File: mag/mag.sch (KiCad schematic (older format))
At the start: 17 parts

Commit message: есть схема макета, начал распологать элементы
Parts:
- removed VD? (x2): S13_SOD-123, N_VD_HL:Диод_S13_SOD-123, symbol elements:Диод_шоттки
- added C5: 10мкФ_0603, N_RLC:Конденсатор_SMD_0603, symbol elements:Конденсатор_керамический
- added K1, K2: кнопка_FSMSM, N_X:Кнопка_FSMSM, symbol elements:кнопка
- added R3, R4, R5: 20k_0603, N_RLC:Конденсатор_SMD_0603, symbol elements:Резистор_0,065Вт
- added VD1: display_EDS803_EDS805, N_VD_HL:display_EDS803_805, symbol elements:display_EDS803_EDS805
- added XP1: Вилка_PLS3, N_X:Розетка_PBS3_вертикальная, symbol elements:Вилка_PLS3
- added XP2: Вилка_PLS6, N_X:Вилка_PLS6_вертикальная, symbol elements:Вилка_PLS6
- DD2, DD3, DD4, DD5: renamed from DD?; value D-triger_8bit -> D-triger_74VHC573MTC
- XS1: renamed from XS?; value Розетка_PBS4 -> oled_0.91_128x32; footprint (none) -> N_VD_HL:oled_0.91_128x32
- XS2: renamed from XS?; footprint (none) -> N_X:Вилка_PLS4_вертикальная
- XТ1: renamed from XТ?; footprint N_X:Клеммник_х2_шаг2.54 -> N_X:батарейный_отсек_CR2032
- gave numbers to parts that had none: 8
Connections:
- net labels added: ADC6, AREF, MC_RX, MC_TX, Out11, Out12, Out13, Out14, Out15, Out16, Out17, Out18, Out21, Out22, Out23, Out24, Out25, Out26, Out27, Out28, Out31, Out32, Out33, Out34, Out35, Out36, Out37, Out38, Out41, Out42, Out43, Out44, Out45, Out46, Out47, Out48, PC0, PC1, PC2, PC3, PD2, PD3, PD4, VCC_bat, VCC_prog
- wire segments 101 -> 207
- no-connect marks 0 -> 5
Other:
- note added: "Информация"
- note added: "Режим/Работа"
- moved on the sheet: C1, C2, C3, C4, DD1, R1, R2, XP3, XТ1

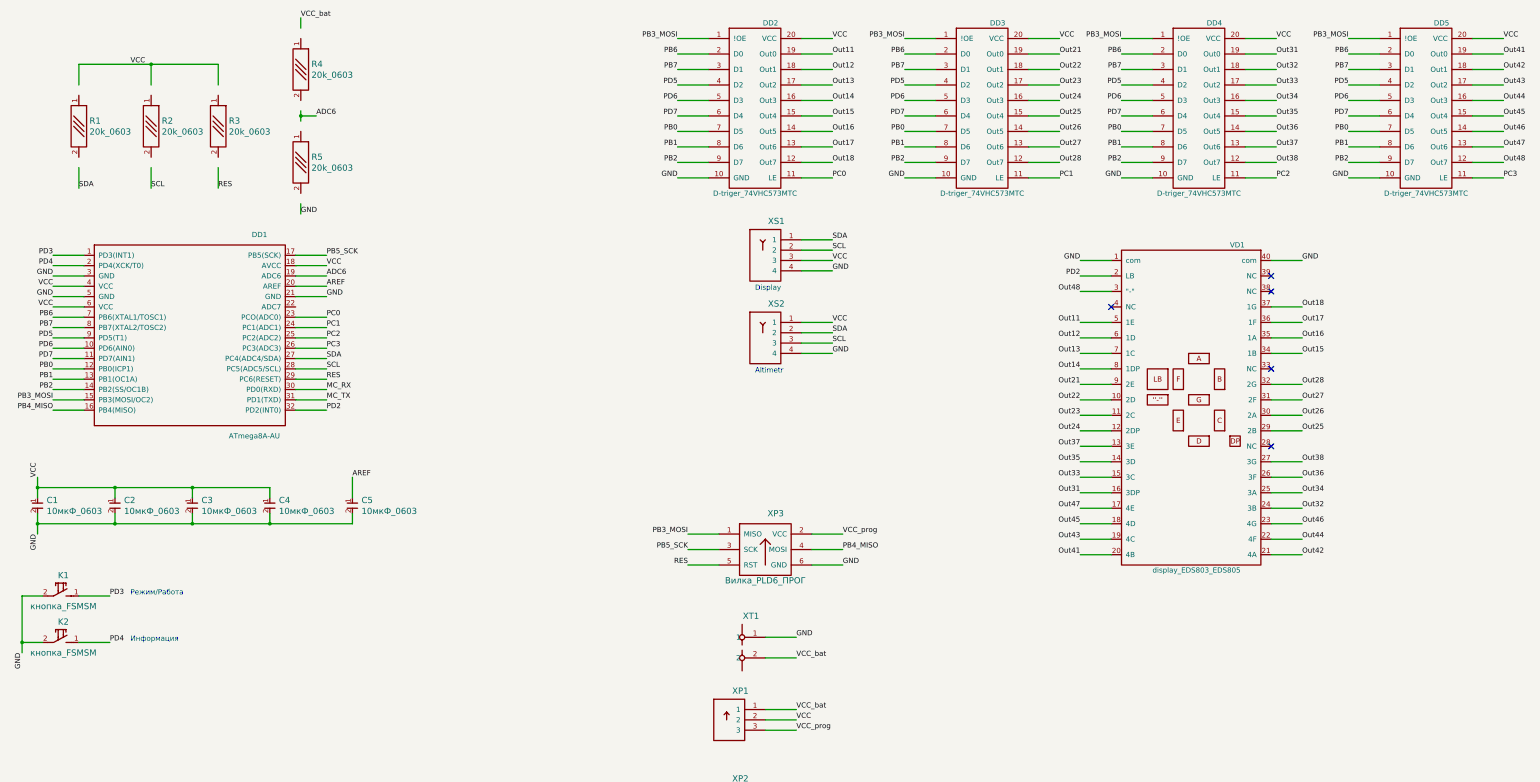
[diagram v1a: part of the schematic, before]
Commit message: есть топология и габарит, не расставлен обвес
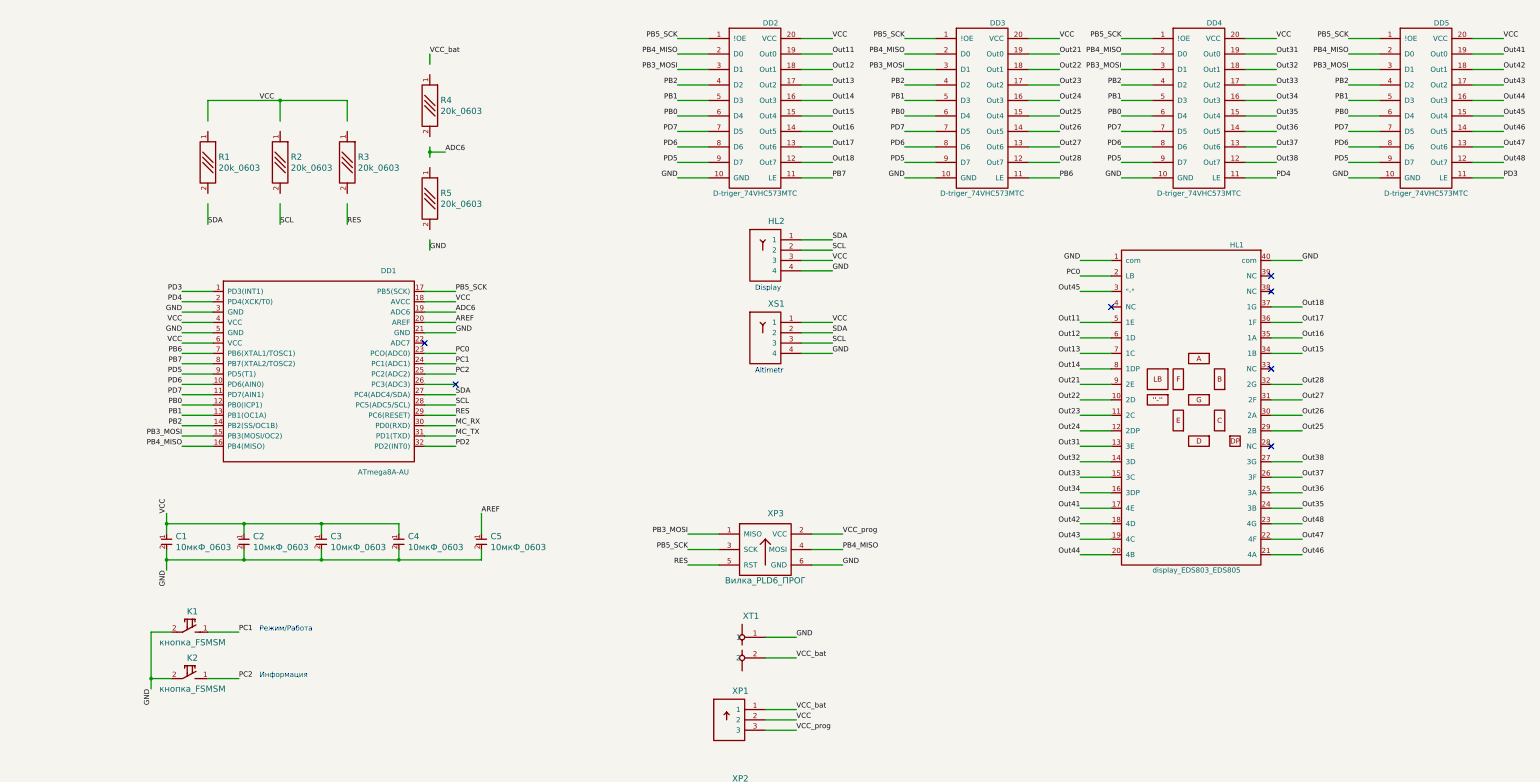
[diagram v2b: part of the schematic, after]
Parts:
- renumbered VD1 to HL1, XS1 to HL2, XS2 to XS1
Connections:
- net labels removed: PC3
- no-connect marks 5 -> 7
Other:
- moved on the sheet: C1, C2, C3, C4, C5, DD1, K1, K2, R1, R2, R3, R4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

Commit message: закончена трассировка и маркировка
не подготавливались файлы производства
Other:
- moved on the sheet: DD2, DD3
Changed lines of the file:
@@
 L elements:D-triger_8bit DD2
 U 1 1 5CE49B21
-P 8200 950
-F 0 "DD2" H 8600 1100 50  0000 C CNN
-F 1 "D-triger_74VHC573MTC" H 8450 -550 50  0000 C CNN
-F 2 "N_DD:SSOP-20" H 8200 950 50  0001 C CNN
-F 3 "" H 8200 950 50  0001 C CNN
-	1    8200 950
+P 8100 950
+F 0 "DD2" H 8500 1100 50  0000 C CNN
+F 1 "D-triger_74VHC573MTC" H 8350 -550 50  0000 C CNN
+F 2 "N_DD:SSOP-20" H 8100 950 50  0001 C CNN
+F 3 "" H 8100 950 50  0001 C CNN
+	1    8100 950
 	1    0    0    -1
 $EndComp
@@
 PB2
 Wire Wire Line
-	8000 1100 7700 1100
-Wire Wire Line
-	8000 1250 7700 1250
-Wire Wire Line
-	8000 1400 7700 1400
-Wire Wire Line
-	8000 1550 7700 1550
-Wire Wire Line
-	8000 1700 7700 1700
-Wire Wire Line
-	8000 1850 7700 1850
-Wire Wire Line
-	8000 2000 7700 2000
-Wire Wire Line
-	8000 2150 7700 2150
+	7900 1100 7600 1100
+Wire Wire Line
+	7900 1250 7600 1250
+Wire Wire Line
+	7900 1400 7600 1400
+Wire Wire Line
+	7900 1550 7600 1550
+Wire Wire Line
+	7900 1700 7600 1700
+Wire Wire Line
+	7900 1850 7600 1850
+Wire Wire Line
+	7900 2000 7600 2000
+Wire Wire Line
+	7900 2150 7600 2150
 Wire Wire Line
 	3200 3600 2900 3600
@@
 VCC
 Wire Wire Line
-	8000 2300 7700 2300
-Text Label 7700 2300 2    50   ~ 0
-GND
-Wire Wire Line
-	9200 950  8900 950
-Text Label 9200 950  0    50   ~ 0
-VCC
-Wire Wire Line
-	8000 950  7700 950
+	7900 2300 7600 2300
+Text Label 7600 2300 2    50   ~ 0
+GND
+Wire Wire Line
+	9100 950  8800 950
+Text Label 9100 950  0    50   ~ 0
+VCC
+Wire Wire Line
+	7900 950  7600 950
 Wire Wire Line
 	8900 2900 9200 2900
@@
 L elements:D-triger_8bit DD3
 U 1 1 5CE59956
-P 10400 950
-F 0 "DD3" H 10800 1100 50  0000 C CNN
-F 1 "D-triger_74VHC573MTC" H 10650 -550 50  0000 C CNN
-F 2 "N_DD:SSOP-20" H 10400 950 50  0001 C CNN
-F 3 "" H 10400 950 50  0001 C CNN
-	1    10400 950
-	1    0    0    -1
-$EndComp
-Wire Wire Line
-	10200 1100 9900 1100
-Wire Wire Line
-	10200 1250 9900 1250
-Wire Wire Line
-	10200 1400 9900 1400
-Wire Wire Line
-	10200 1550 9900 1550
-Wire Wire Line
-	10200 1700 9900 1700
-Wire Wire Line
-	10200 1850 9900 1850
-Wire Wire Line
-	10200 2000 9900 2000
-Wire Wire Line
-	10200 2150 9900 2150
-Wire Wire Line
-	10200 2300 9900 2300
-Wire Wire Line
-	11400 950  11100 950
-Text Label 11400 950  0    50   ~ 0
-VCC
-Wire Wire Line
-	10200 950  9900 950
+P 10300 950
+F 0 "DD3" H 10700 1100 50  0000 C CNN
+F 1 "D-triger_74VHC573MTC" H 10550 -550 50  0000 C CNN
+F 2 "N_DD:SSOP-20" H 10300 950 50  0001 C CNN
+F 3 "" H 10300 950 50  0001 C CNN
+	1    10300 950
+	1    0    0    -1
+$EndComp
+Wire Wire Line
+	10100 1100 9800 1100
+Wire Wire Line
+	10100 1250 9800 1250
+Wire Wire Line
+	10100 1400 9800 1400
+Wire Wire Line
+	10100 1550 9800 1550
+Wire Wire Line
+	10100 1700 9800 1700
+Wire Wire Line
+	10100 1850 9800 1850
+Wire Wire Line
+	10100 2000 9800 2000
+Wire Wire Line
+	10100 2150 9800 2150
+Wire Wire Line
+	10100 2300 9800 2300
+Wire Wire Line
+	11300 950  11000 950
+Text Label 11300 950  0    50   ~ 0
+VCC
+Wire Wire Line
+	10100 950  9800 950
 $Comp
 L elements:D-triger_8bit DD4
@@
 NoConn ~ 13450 4900
 Wire Wire Line
-	9200 1100 8900 1100
-Text Label 9200 1100 0    50   ~ 0
+	9100 1100 8800 1100
+Text Label 9100 1100 0    50   ~ 0
 Out11
 Wire Wire Line
-	9200 1250 8900 1250
-Text Label 9200 1250 0    50   ~ 0
+	9100 1250 8800 1250
+Text Label 9100 1250 0    50   ~ 0
 Out12
 Wire Wire Line
-	9200 1400 8900 1400
-Text Label 9200 1400 0    50   ~ 0
+	9100 1400 8800 1400
+Text Label 9100 1400 0    50   ~ 0
 Out13
 Wire Wire Line
-	9200 1550 8900 1550
-Text Label 9200 1550 0    50   ~ 0
+	9100 1550 8800 1550
+Text Label 9100 1550 0    50   ~ 0
 Out14
 Wire Wire Line
-	9200 1700 8900 1700
-Text Label 9200 1700 0    50   ~ 0
+	9100 1700 8800 1700
+Text Label 9100 1700 0    50   ~ 0
 Out15
 Wire Wire Line
-	9200 1850 8900 1850
-Text Label 9200 1850 0    50   ~ 0
+	9100 1850 8800 1850
+Text Label 9100 1850 0    50   ~ 0
 Out16
 Wire Wire Line
-	9200 2000 8900 2000
-Text Label 9200 2000 0    50   ~ 0
+	9100 2000 8800 2000
+Text Label 9100 2000 0    50   ~ 0
 Out17
 Wire Wire Line
-	9200 2150 8900 2150
-Text Label 9200 2150 0    50   ~ 0
+	9100 2150 8800 2150
+Text Label 9100 2150 0    50   ~ 0
 Out18
 Wire Wire Line
-	11400 1100 11100 1100
-Text Label 11400 1100 0    50   ~ 0
+	11300 1100 11000 1100
+Text Label 11300 1100 0    50   ~ 0
 Out21
 Wire Wire Line
-	11400 1250 11100 1250
-Text Label 11400 1250 0    50   ~ 0
+	11300 1250 11000 1250
+Text Label 11300 1250 0    50   ~ 0
 Out22
 Wire Wire Line
-	11400 1400 11100 1400
-Text Label 11400 1400 0    50   ~ 0
+	11300 1400 11000 1400
+Text Label 11300 1400 0    50   ~ 0
 Out23
 Wire Wire Line
-	11400 1550 11100 1550
-Text Label 11400 1550 0    50   ~ 0
+	11300 1550 11000 1550
+Text Label 11300 1550 0    50   ~ 0
 Out24
 Wire Wire Line
-	11400 1700 11100 1700
-Text Label 11400 1700 0    50   ~ 0
+	11300 1700 11000 1700
+Text Label 11300 1700 0    50   ~ 0
 Out25
 Wire Wire Line
-	11400 1850 11100 1850
-Text Label 11400 1850 0    50   ~ 0
+	11300 1850 11000 1850
+Text Label 11300 1850 0    50   ~ 0
 Out26
 Wire Wire Line
-	11400 2000 11100 2000
-Text Label 11400 2000 0    50   ~ 0
+	11300 2000 11000 2000
+Text Label 11300 2000 0    50   ~ 0
 Out27
 Wire Wire Line
-	11400 2150 11100 2150
-Text Label 11400 2150 0    50   ~ 0
+	11300 2150 11000 2150
+Text Label 11300 2150 0    50   ~ 0
 Out28
 Wire Wire Line
@@
 	13500 2300 13200 2300
 Wire Wire Line
-	11400 2300 11100 2300
-Wire Wire Line
-	9200 2300 8900 2300
+	11300 2300 11000 2300
+Wire Wire Line
+	9100 2300 8800 2300
 $Comp
 L elements:кнопка K1
@@
 Text Label 13750 4450 0    50   ~ 0
 Out27
-Text Label 7700 1250 2    50   ~ 0
+Text Label 7600 1250 2    50   ~ 0
 PB3_MOSI
-Text Label 7700 2150 2    50   ~ 0
+Text Label 7600 2150 2    50   ~ 0
 PD5
-Text Label 7700 2000 2    50   ~ 0
+Text Label 7600 2000 2    50   ~ 0
 PD6
-Text Label 7700 1850 2    50   ~ 0
+Text Label 7600 1850 2    50   ~ 0
 PD7
-Text Label 7700 1700 2    50   ~ 0
+Text Label 7600 1700 2    50   ~ 0
 PB0
-Text Label 7700 1550 2    50   ~ 0
+Text Label 7600 1550 2    50   ~ 0
 PB1
-Text Label 7700 1400 2    50   ~ 0
+Text Label 7600 1400 2    50   ~ 0
 PB2
-Text Label 7700 1100 2    50   ~ 0
+Text Label 7600 1100 2    50   ~ 0
 PB4_MISO
-Text Label 7700 950  2    50   ~ 0
+Text Label 7600 950  2    50   ~ 0
 PB5_SCK
-Text Label 9900 2300 2    50   ~ 0
-GND
-Text Label 9900 1250 2    50   ~ 0
+Text Label 9800 2300 2    50   ~ 0
+GND
+Text Label 9800 1250 2    50   ~ 0
 PB3_MOSI
-Text Label 9900 2150 2    50   ~ 0
+Text Label 9800 2150 2    50   ~ 0
 PD5
-Text Label 9900 2000 2    50   ~ 0
+Text Label 9800 2000 2    50   ~ 0
 PD6
-Text Label 9900 1850 2    50   ~ 0
+Text Label 9800 1850 2    50   ~ 0
 PD7
-Text Label 9900 1700 2    50   ~ 0
+Text Label 9800 1700 2    50   ~ 0
 PB0
-Text Label 9900 1550 2    50   ~ 0
+Text Label 9800 1550 2    50   ~ 0
 PB1
-Text Label 9900 1400 2    50   ~ 0
+Text Label 9800 1400 2    50   ~ 0
 PB2
-Text Label 9900 1100 2    50   ~ 0
+Text Label 9800 1100 2    50   ~ 0
 PB4_MISO
-Text Label 9900 950  2    50   ~ 0
+Text Label 9800 950  2    50   ~ 0
 PB5_SCK
 Text Label 12000 2300 2    50   ~ 0
@@
 Text Label 2900 4000 2    50   ~ 0
 PB6
-Text Label 11400 2300 0    50   ~ 0
+Text Label 11300 2300 0    50   ~ 0
 PB6
-Text Label 9200 2300 0    50   ~ 0
+Text Label 9100 2300 0    50   ~ 0
 PB7
 Text Label 2900 4100 2    50   ~ 0

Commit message: готово отображение на lcd
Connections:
- no-connect marks 7 -> 8
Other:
- note added: "поменять out44 и out45"
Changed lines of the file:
@@
 PC2
 NoConn ~ 5550 4300
+NoConn ~ 5850 4900
+Text Notes 14650 5900 0    50   ~ 0
+поменять out44 и out45
 $EndSCHEMATC

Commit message: подготавливается переделка под стационарные датчики
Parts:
- removed XТ1: Клеммник_х2, N_X:батарейный_отсек_CR2032, symbol elements:Клеммник_х2
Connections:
- wire segments 207 -> 205
- no-connect marks 8 -> 7
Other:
- note removed: "поменять out44 и out45"
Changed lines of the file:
@@
 Altimetr
-$Comp
-L elements:Клеммник_х2 XТ1
-U 1 1 5CE694BC
-P 8550 6750
-F 0 "XТ1" H 8411 6956 60  0000 C CNN
-F 1 "Клеммник_х2" H 8500 6375 60  0001 C CNN
-F 2 "N_X:батарейный_отсек_CR2032" H 8550 6750 60  0001 C CNN
-F 3 "" H 8550 6750 60  0001 C CNN
-	1    8550 6750
-	1    0    0    -1
-$EndComp
-Wire Wire Line
-	8850 6750 8550 6750
-Text Label 8850 6750 0    50   ~ 0
-GND
 $Comp
 L elements:Конденсатор_керамический C1
@@
 Text Label 11600 5800 2    50   ~ 0
 Out43
-Text Label 11600 3400 2    50   ~ 0
+Text Label 11600 5950 2    50   ~ 0
 Out45
 Text Label 13750 5800 0    50   ~ 0
@@
 Text Label 11600 5650 2    50   ~ 0
 Out42
-Text Label 11600 5950 2    50   ~ 0
+Text Label 11600 3400 2    50   ~ 0
 Out44
 Text Label 13750 5950 0    50   ~ 0
@@
 Wire Wire Line
 	9300 5750 9000 5750
-Text Label 8850 6950 0    50   ~ 0
-VCC_bat
-Wire Wire Line
-	8550 6950 8850 6950
 Text Label 8850 7450 0    50   ~ 0
 VCC_bat
@@
 PC2
 NoConn ~ 5550 4300
-NoConn ~ 5850 4900
-Text Notes 14650 5900 0    50   ~ 0
-поменять out44 и out45
 $EndSCHEMATC

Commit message: выложена схема питания и преобразователя
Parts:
- removed XS1: Розетка_PBS4, N_X:Вилка_PLS4_вертикальная, symbol elements:Розетка_PBS4
- added X1: Клеммник_х2, N_X:Вилка_PLS2_вертикальная, symbol elements:Клеммник_х2
- added XP4: USB_female, N_X:Вилка_PLS4_вертикальная, symbol elements:Вилка_PLS4
- C1, C2, C3, C4, C5: value 10мкФ_0603 -> Конденсатор_керамический; Номинал (none) -> 10 мкФ/6,3 В; УГО (none) -> С111
- DD1: value ATmega8A-AU -> ATmega328
- R1, R2, R3, R4, R5: value 20k_0603 -> Резистор_0,065Вт; Номинал (none) -> 20 кОм; УГО (none) -> R101
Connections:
- net labels added: 3V, RX(MISO), TX(MOSI), USB_D+, USB_D-, gnd
- wire segments 205 -> 227
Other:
- note added: "USB type C"
- note added: "Подключение аккумулятора"
- note removed: "Altimetr"
- moved on the sheet: DD1, DD2, DD3, DD4, DD5, HL1, HL2, K1, K2, R1, R2, R3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

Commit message: на схеме не отражены внешняя i2c-eeprom
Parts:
- removed XP1: Вилка_PLS3, N_X:Розетка_PBS3_вертикальная, symbol elements:Вилка_PLS3
- removed XP2: Вилка_PLS6, N_X:Вилка_PLS6_вертикальная, symbol elements:Вилка_PLS6
- added R15, R16, R17, R18, R19, R20: Резистор_0,065Вт, N_RLC:Конденсатор_SMD_0603, symbol elements:Резистор_0,065Вт
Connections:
- net MC_RX is gone; now on net TX(MOSI): DD1.30 (PD0(RXD))
- net MC_TX is gone; now on net RX(MISO): DD1.31 (PD1(TXD))
- net 3V: now also HL2.3, R17.2
- net ADC6: now also R4.2, R5.1
- net AREF: now also R17.1
- net GND: no longer C1.2, C2.2, C3.2, C4.2, C5.2, DD1.3 (GND), DD1.5 (GND), HL2.4, XP3.6 (GND)
- net PB3_MOSI: now also R20.1; no longer XP3.1 (MISO)
- net PB4_MISO: now also R18.1; no longer XP3.4 (MOSI)
- net PB5_SCK: now also R19.1; no longer XP3.3 (SCK)
- net PC1: now also R15.2
- net PC2: now also R16.2
- net VCC_bat: now also C1.1, C2.1, C3.1, C4.1, DD1.18 (AVCC), DD1.4 (VCC), DD1.6 (VCC), R1.1, R2.1, R3.1, R4.1, R15.1, R16.1
- net gnd: now also C1.2, C2.2, C3.2, C4.2, C5.2, DD1.3 (GND), DD1.5 (GND), HL2.4, R5.2, XP3.6 (GND)
- net PC3: now reaches DD1.26 (PC3(ADC3))
- removed net VCC: C1.1, C2.1, C3.1, C4.1, DD1.18 (AVCC), DD1.4 (VCC), DD1.6 (VCC), DD2.20 (VCC), DD3.20 (VCC), DD4.20 (VCC), DD5.20 (VCC), HL2.3, R1.1, R2.1, R3.1
- net VCC_prog: no longer names the net of XP3.2 (VCC)
- new net: R18.2, XP3.1 (MISO)
- new net: R19.2, XP3.3 (SCK)
- new net: R20.2, XP3.4 (MOSI)
- new net 5V: DD2.20 (VCC), DD3.20 (VCC), DD4.20 (VCC), DD5.20 (VCC)
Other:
- moved on the sheet: C1, C2, C3, C4, C5, DD1, DD2, DD3, DD4, DD5, HL1, HL2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

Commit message: закончена около-боевая разводка, на плате оставлены штыревые разъемы
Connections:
- net GND is gone; now on net gnd: DD1.21 (GND), DD2.10 (GND), DD3.10 (GND), DD4.10 (GND), DD5.10 (GND), HL1.1 (com), HL1.40 (com), K1.2, K2.2
- net PD2: no longer names the net of DD1.32 (PD2(INT0))
- no-connect marks 7 -> 8
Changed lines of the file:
@@
 Wire Wire Line
 	7200 5850 6900 5850
-Text Label 6900 5850 2    50   ~ 0
-GND
 Wire Wire Line
 	8400 4500 8100 4500
@@
 Wire Wire Line
 	13650 1000 13350 1000
-Text Label 13350 1000 2    50   ~ 0
-GND
 Wire Wire Line
 	15500 1000 15200 1000
-Text Label 15500 1000 0    50   ~ 0
-GND
 NoConn ~ 15200 1150
 NoConn ~ 15200 1300
@@
 Text Label 2000 6600 2    50   ~ 0
 PD4
-Text Label 1500 9350 3    50   ~ 0
-GND
 Wire Wire Line
 	1500 9250 1500 9350
@@
 	13350 1150 13650 1150
 Wire Wire Line
-	4350 8000 4650 8000
-Text Label 4650 8000 0    50   ~ 0
-PD2
-Wire Wire Line
 	4350 6900 4650 6900
-Text Label 4650 6900 0    50   ~ 0
-GND
 Wire Wire Line
 	4350 6600 4650 6600
@@
 Text Label 6900 4500 2    50   ~ 0
 PB5_SCK
-Text Label 9100 5850 2    50   ~ 0
-GND
 Text Label 9100 4800 2    50   ~ 0
 PB3_MOSI
@@
 Text Label 9100 4500 2    50   ~ 0
 PB5_SCK
-Text Label 11300 5850 2    50   ~ 0
-GND
 Text Label 11300 4800 2    50   ~ 0
 PB3_MOSI
@@
 Text Label 11300 4500 2    50   ~ 0
 PB5_SCK
-Text Label 13500 5850 2    50   ~ 0
-GND
 Text Label 13500 4800 2    50   ~ 0
 PB3_MOSI
@@
 F4 "I2C_SDA" I L 9500 2000 50
 F5 "I2C_SCL" I L 9500 2250 50
+F6 "VCCbat" I R 10500 1750 50
 $EndSheet
 Wire Wire Line
@@
 Wire Wire Line
 	5000 2750 5250 2750
+Text Label 4650 6900 0    50   ~ 0
+gnd
+Text Label 13500 5850 2    50   ~ 0
+gnd
+Text Label 11300 5850 2    50   ~ 0
+gnd
+Text Label 9100 5850 2    50   ~ 0
+gnd
+Text Label 6900 5850 2    50   ~ 0
+gnd
+Text Label 13350 1000 2    50   ~ 0
+gnd
+Text Label 15500 1000 0    50   ~ 0
+gnd
+NoConn ~ 4350 8000
+Text Label 1500 9350 3    50   ~ 0
+gnd
+Text Label 10750 1750 0    50   ~ 0
+VCC_bat
+Wire Wire Line
+	10500 1750 10750 1750
 $EndSCHEMATC
